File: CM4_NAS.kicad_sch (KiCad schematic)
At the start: 32 parts, among them J1 USB_A, J10 Conn_02x07_Odd_Even, J11 Conn_01x03, J12 Conn_01x03, J13 Conn_02x06_Odd_Even, J15 Temp_Sensor, J2 HDMI_header, J3 PCIe_conn, J4 Sata_PWR, J5 PWR_IN, J6 12-3.3_BUCK, J7 Fan_conn, J8 OLED_conn, J9 Conn_01x03, U1 74LVC1G07SE-7, U2 TPD4EUSB30, U3 TPD4EUSB30, U4 MagJack-0826-1G1T-43-F, U5 TPD4EUSB30, U6 EMC2301-1-ACZL-TR, U7 74LVC1G07SE-7

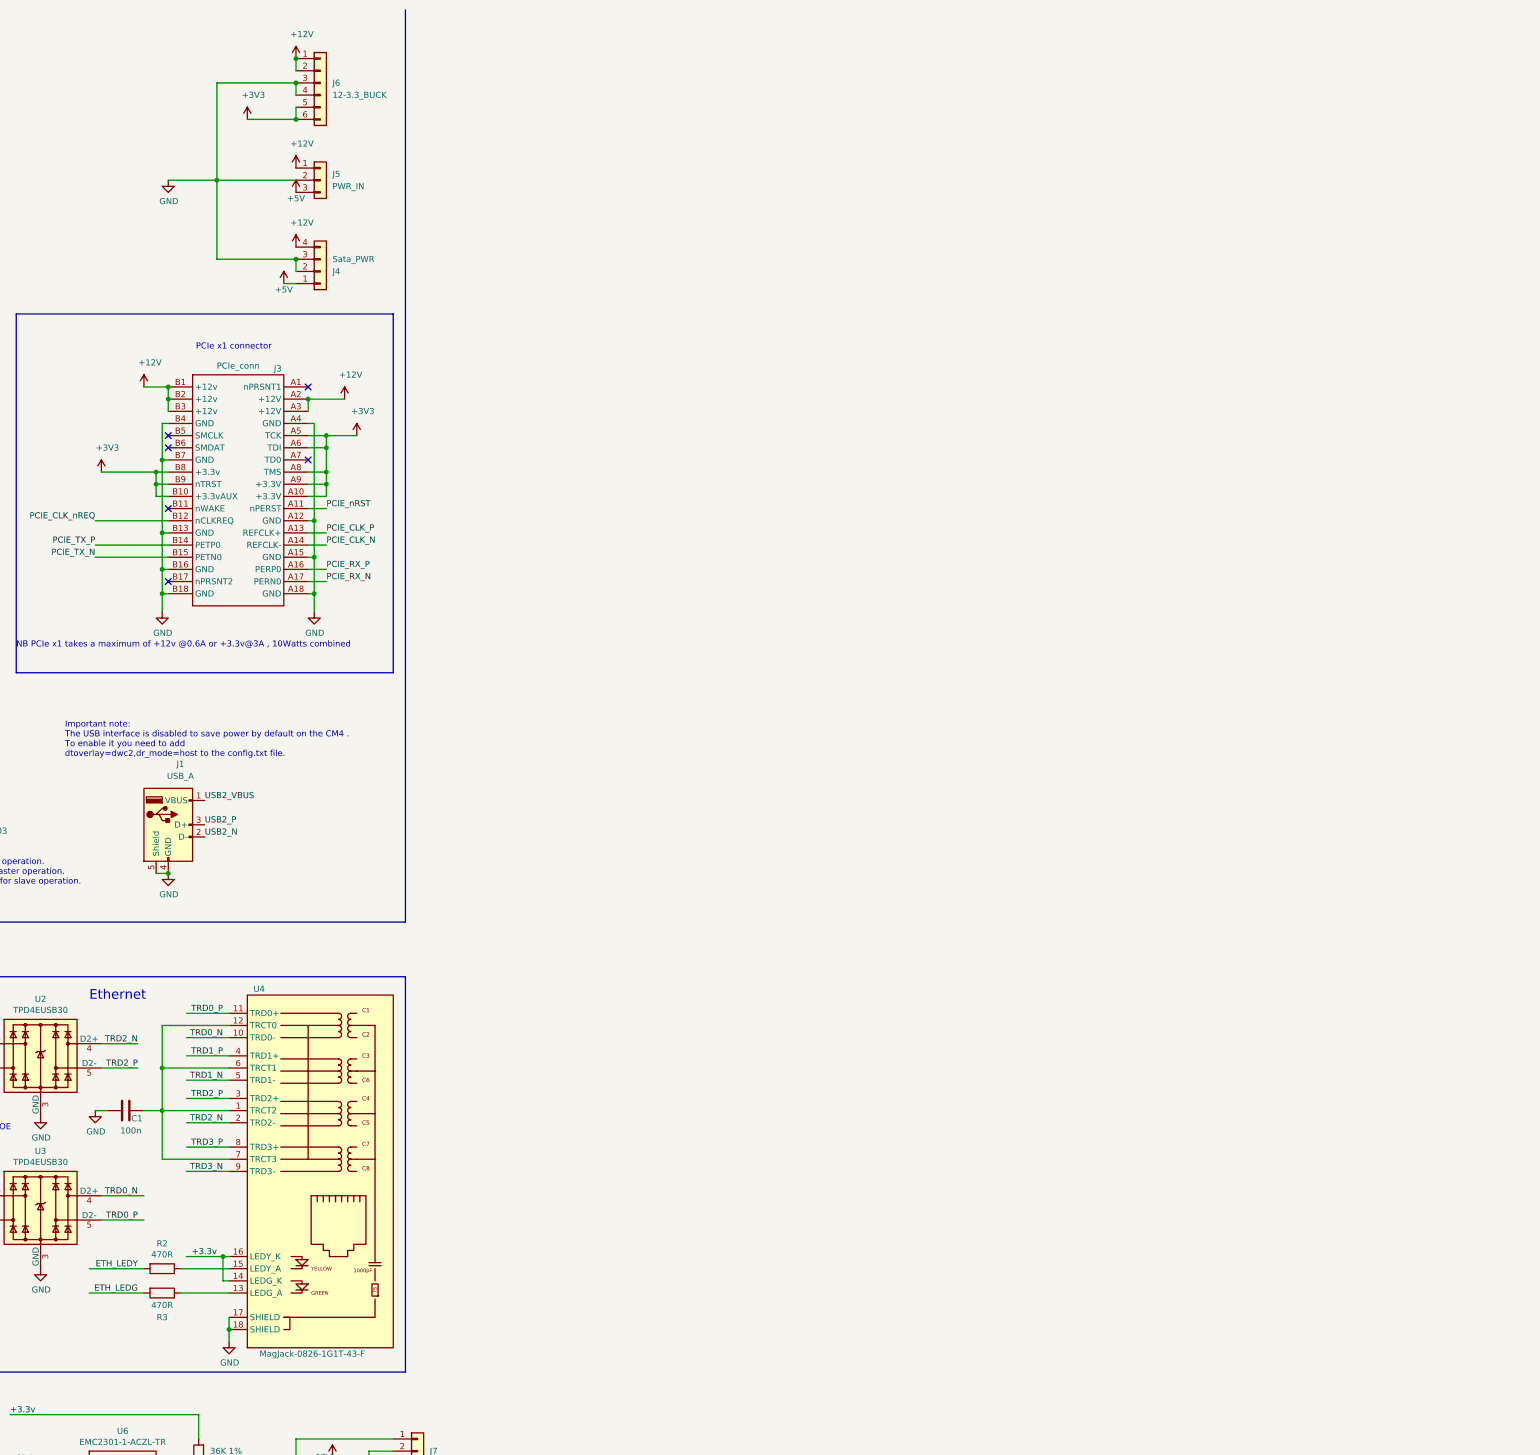
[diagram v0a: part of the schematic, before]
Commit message: Updated to Version 1.5, imported power circuitry for 12V input only
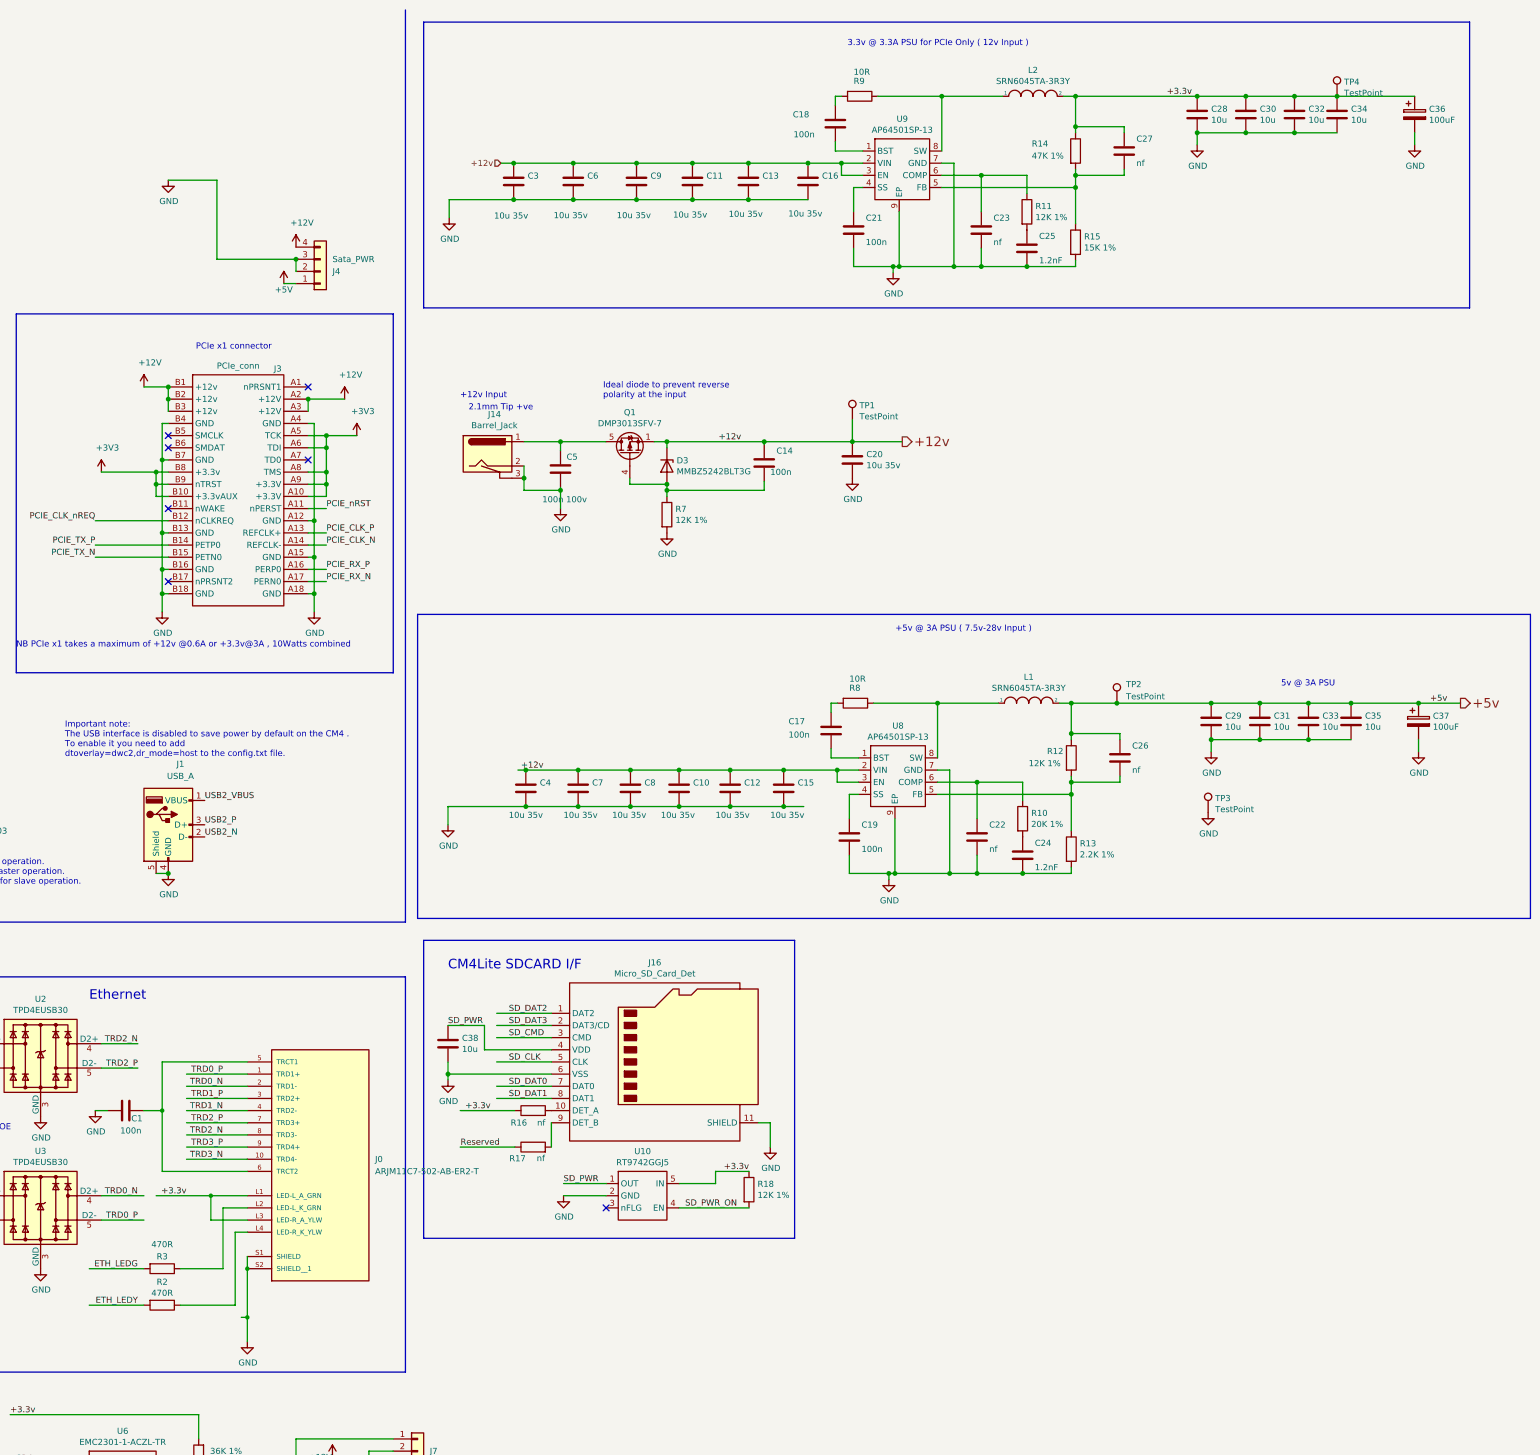
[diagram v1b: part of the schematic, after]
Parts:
- removed J5: PWR_IN, Connector_JST:JST_XH_B3B-XH-A_1x03_P2.50mm_Vertical, symbol Connector_Generic:Conn_01x03
- removed J6: 12-3.3_BUCK, Connector_PinSocket_2.54mm:PinSocket_1x06_P2.54mm_Vertical, symbol Connector_Generic:Conn_01x06
- removed U4: MagJack-0826-1G1T-43-F, CM4:MagJack_0826-1G1T-43-F, symbol CM4_NAS:MagJack-0826-1G1T-43-F
- added C10, C11, C12, C13, C15, C16, C20, C3, C4, C6, C7, C8, C9: 10u 35v, Capacitor_SMD:C_0805_2012Metric, symbol Device:C
- added C14, C17, C18, C19, C21: 100n, Capacitor_SMD:C_0402_1005Metric, symbol Device:C
- added C22, C23, C26, C27: nf, Capacitor_SMD:C_0402_1005Metric, symbol Device:C
- added C24, C25: 1.2nF, Capacitor_SMD:C_0402_1005Metric, symbol Device:C
- added C28, C29, C30, C31, C32, C33, C34, C35, C38: 10u, Capacitor_SMD:C_0805_2012Metric, symbol Device:C
- added C36, C37: 100uF, Capacitor_Tantalum_SMD:CP_EIA-7343-31_Kemet-D, symbol Device:CP
- added C5: 100n 100v, Capacitor_SMD:C_0402_1005Metric, symbol Device:C
- added D3: MMBZ5242BLT3G, Diode_SMD:D_SOT-23_ANK, symbol Diode:BZX84Cxx
- added J0: ARJM11C7-502-AB-ER2-T, CM4:ABRACON_ARJM11C7-502-AB-ER2-T, symbol Eth:ARJM11C7-502-AB-ER2-T
- added J14: Barrel_Jack, CM4:BarrelJack_Horizontal, symbol CM4IO:Barrel_Jack
- added J16: Micro_SD_Card_Det, CM4:SDCARD_MOLEX_503398-1892, symbol Connector:Micro_SD_Card_Det
- added L1, L2: SRN6045TA-3R3Y, Inductor_SMD:L_Bourns_SRN6045TA, symbol pspice:INDUCTOR
- added Q1: DMP3013SFV-7, Package_SON:Diodes_PowerDI3333-8, symbol Transistor_FET:DMP3013SFV
- added R10: 20K 1%, Resistor_SMD:R_0402_1005Metric, symbol Device:R
- added R11, R12, R18, R7: 12K 1%, Resistor_SMD:R_0402_1005Metric, symbol Device:R
- added R13: 2.2K 1%, Resistor_SMD:R_0402_1005Metric, symbol Device:R
- added R14: 47K 1%, Resistor_SMD:R_0402_1005Metric, symbol Device:R
- added R15: 15K 1%, Resistor_SMD:R_0402_1005Metric, symbol Device:R
- added R16, R17: nf, Resistor_SMD:R_0402_1005Metric, symbol Device:R
- added R8, R9: 10R, Resistor_SMD:R_0402_1005Metric, symbol Device:R
- added TP1, TP2, TP3, TP4: TestPoint, TestPoint:TestPoint_Pad_2.0x2.0mm, symbol Connector:TestPoint
- added U10: RT9742GGJ5, Package_TO_SOT_SMD:SOT-23-5, symbol CM4IO:RT9742GGJ5
- added U8, U9: AP64501SP-13, CM4:SOIC-8-1EP_3.9x4.9mm_P1.27mm_EP2.95x4.9mm_Mask2.71x3.4mm_ThermalVias, symbol CM4IO:AP64351
- R1, R2, R3, R4, R5, R6: footprint Resistor_THT:R_Axial_DIN0207_L6.3mm_D2.5mm_P7.62mm_Horizontal -> Resistor_SMD:R_0402_1005Metric
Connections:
- net +3.3v: now also C27.1, C28.1, C30.1, C32.1, C34.1, C36.1, J0.L1 (LED-L_A_GRN), J0.L3 (LED-R_A_YLW), L2.2, R14.1, R16.1, R18.1, TP4.1, U10.5 (IN)
- net GND: now also C10.2, C11.2, C12.2, C13.2, C15.2, C16.2, C19.2, C20.2, C21.2, C22.2, C23.2, C24.2, C25.2, C28.2, C29.2, C3.2, C30.2, C31.2, C32.2, C33.2, C34.2, C35.2, C36.2, C37.2, C38.2, C4.2, C5.2, C6.2, C7.2, C8.2, C9.2, J0.S1 (SHIELD), J0.S2 (SHIELD__1), J14.2, J14.3, J16.11 (SHIELD), J16.6 (VSS), R13.2, R15.2, R7.2, TP3.1, U10.2 (GND), U8.7 (GND), U8.9 (EP), U9.7 (GND), U9.9 (EP)
- net SD_CLK: now also J16.5 (CLK)
- net SD_CMD: now also J16.3 (CMD)
- net SD_DAT0: now also J16.7 (DAT0)
- net SD_DAT1: now also J16.8 (DAT1)
- net SD_DAT2: now also J16.1 (DAT2)
- net SD_DAT3: now also J16.2 (DAT3/CD)
- net SD_PWR_ON: now also R18.2, U10.4 (EN)
- net TRD0_N: now also J0.2 (TRD1-)
- net TRD0_P: now also J0.1 (TRD1+)
- net TRD1_N: now also J0.4 (TRD2-)
- net TRD1_P: now also J0.3 (TRD2+)
- net TRD2_N: now also J0.8 (TRD3-)
- net TRD2_P: now also J0.7 (TRD3+)
- net TRD3_N: now also J0.10 (TRD4-)
- net TRD3_P: now also J0.9 (TRD4+)
- net at C1.1: now also J0.5 (TRCT1), J0.6 (TRCT2)
- net at R3.1: now also J0.L2 (LED-L_K_GRN)
- net at R2.1: now also J0.L4 (LED-R_K_YLW)
- new net: C14.2, D3.2 (A), Q1.4 (G), R7.1
- new net: C5.1, J14.1, Q1.5 (D)
- new net: C17.2, U8.1 (BST)
- new net: C19.1, U8.4 (SS)
- new net: C26.2, R12.2, R13.1, U8.5 (FB)
- new net: C22.1, R10.1, U8.6 (COMP)
- new net: L1.1, R8.1, U8.8 (SW)
- new net: C23.1, R11.1, U9.6 (COMP)
- new net: C18.2, U9.1 (BST)
- new net: C21.1, U9.4 (SS)
- new net: C27.2, R14.2, R15.1, U9.5 (FB)
- new net: L2.1, R9.1, U9.8 (SW)
- new net: C17.1, R8.2
- new net: C24.1, R10.2
- new net: C18.1, R9.2
- new net: C25.1, R11.2
- new net: J16.10 (DET_A), R16.2
- new net: J16.9 (DET_B), R17.2
- new net +12v: C10.1, C11.1, C12.1, C13.1, C14.1, C15.1, C16.1, C20.1, C3.1, C4.1, C6.1, C7.1, C8.1, C9.1, D3.1 (K), Q1.1 (S), Q1.2 (S), Q1.3 (S), TP1.1, U8.2 (VIN), U8.3 (EN), U9.2 (VIN), U9.3 (EN)
- new net +5v: C26.1, C29.1, C31.1, C33.1, C35.1, C37.1, L1.2, R12.1, TP2.1
- new net Reserved: R17.1
- new net SD_PWR: C38.1, J16.4 (VDD), U10.1 (OUT)
- no-connect marks 17 -> 18
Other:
- note added: "+12v Input"
- note added: "+5v @ 3A PSU ( 7.5v-28v Input )"
- note added: "2.1mm Tip +ve"
- note added: "3.3v @ 3.3A PSU for PCIe Only ( 12v Input )"
- note added: "5v @ 3A PSU"
- note added: "CM4Lite SDCARD I/F"
- note added: "Ideal diode to prevent reverse polarity at the input"
- moved on the sheet: R2, R3
